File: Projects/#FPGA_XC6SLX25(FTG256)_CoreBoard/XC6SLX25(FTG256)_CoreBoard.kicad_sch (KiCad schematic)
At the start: 148 parts, among them J1 MTA18ASF2G72HZ-2G3A1, U1 XC6SLX25-FTG256, U2 W25Q128JVS, U3 TPS51200DRC, U4 MP214x, U5 MP214x, U6 MP214x, U7 MP214x, X1 ECS-2520MV-xxx-xx

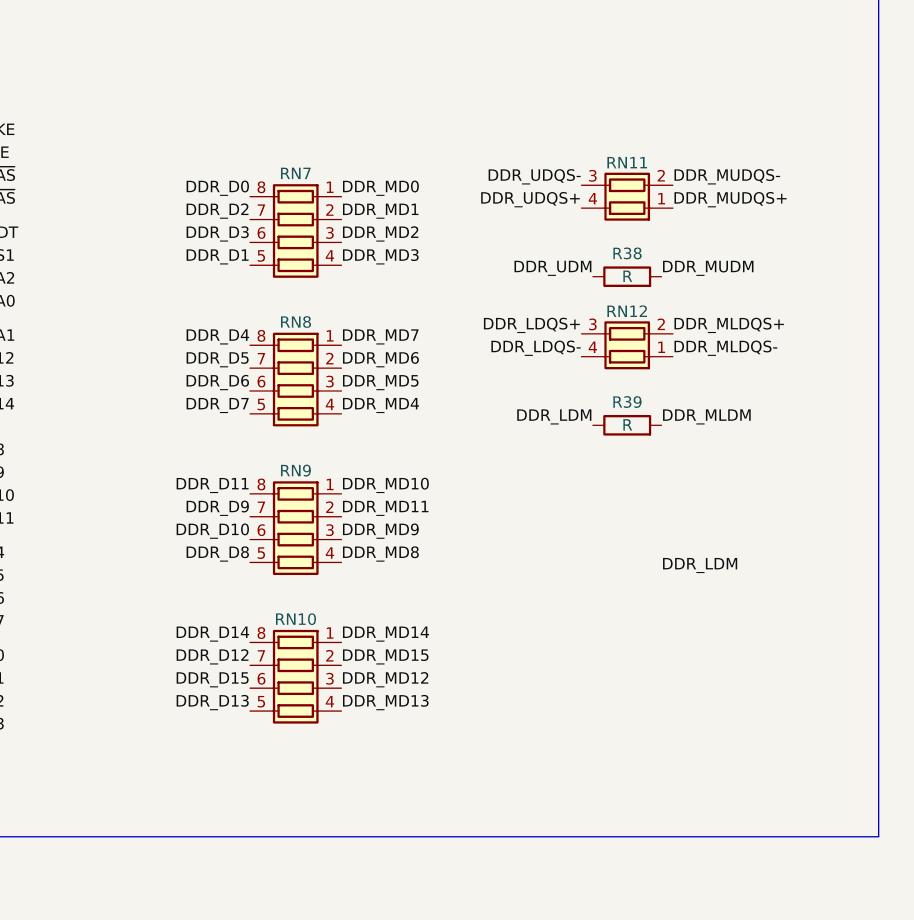
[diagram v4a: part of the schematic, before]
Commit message: Update XC6SLX25(FTG256)_CoreBoard
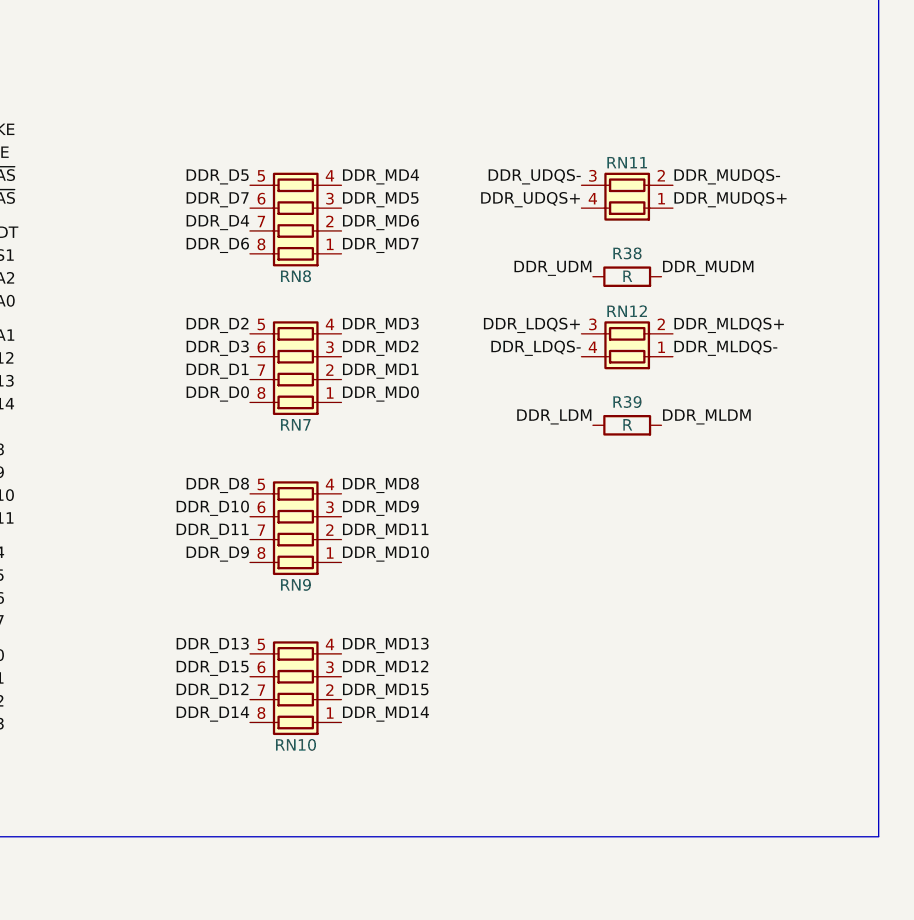
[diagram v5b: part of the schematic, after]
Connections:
- net DDR_D1: now also RN7.7 (R2.2); no longer RN7.5 (R4.2)
- net DDR_D11: now also RN9.7 (R2.2); no longer RN9.8 (R1.2)
- net DDR_D2: now also RN7.5 (R4.2); no longer RN7.7 (R2.2)
- net DDR_D4: now also RN8.7 (R2.2); no longer RN8.8 (R1.2)
- net DDR_D5: now also RN8.5 (R4.2); no longer RN8.7 (R2.2)
- net DDR_D6: now also RN8.8 (R1.2); no longer RN8.6 (R3.2)
- net DDR_D7: now also RN8.6 (R3.2); no longer RN8.5 (R4.2)
- net DDR_D9: now also RN9.8 (R1.2); no longer RN9.7 (R2.2)
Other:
- moved on the sheet: RN10, RN7, RN8

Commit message: Update XC6SLX25(FTG256)_CoreBoard (DDR3 Routing)
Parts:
- removed R38, R39: R, Resistor_SMD:R_0402_1005Metric, symbol Device:R
- added RN13: R_Pack02, Resistor_SMD:R_Array_Convex_2x0402, symbol Device:R_Pack02
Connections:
- net DDR_A1: now also RN2.5 (R4.2); no longer RN1.7 (R2.2)
- net DDR_A10: now also RN5.5 (R4.2); no longer RN3.6 (R3.2)
- net DDR_A11: now also RN2.7 (R2.2); no longer RN3.5 (R4.2)
- net DDR_A12: now also RN2.8 (R1.2); no longer RN4.7 (R2.2)
- net DDR_A13: now also RN1.7 (R2.2); no longer RN4.6 (R3.2)
- net DDR_A14: now also RN2.6 (R3.2); no longer RN4.5 (R4.2)
- net DDR_A2: now also RN1.5 (R4.2); no longer RN1.6 (R3.2)
- net DDR_A3: now also RN6.6 (R3.2); no longer RN1.5 (R4.2)
- net DDR_A4: now also RN4.6 (R3.2); no longer RN2.8 (R1.2)
- net DDR_A5: now also RN6.7 (R2.2); no longer RN2.7 (R2.2)
- net DDR_A6: now also RN4.7 (R2.2); no longer RN2.6 (R3.2)
- net DDR_A7: now also RN6.8 (R1.2); no longer RN2.5 (R4.2)
- net DDR_A8: now also RN4.8 (R1.2); no longer RN3.8 (R1.2)
- net DDR_A9: now also RN1.6 (R3.2); no longer RN3.7 (R2.2)
- net DDR_BA0: now also RN6.5 (R4.2); no longer RN5.5 (R4.2)
- net DDR_BA1: now also RN4.5 (R4.2); no longer RN4.8 (R1.2)
- net DDR_CKE: now also RN3.8 (R1.2); no longer RN6.8 (R1.2)
- net DDR_LDM: now also RN13.4 (R1.2)
- net DDR_MLDM: now also RN13.1 (R1.1)
- net DDR_MUDM: now also RN13.2 (R2.1)
- net DDR_UDM: now also RN13.3 (R2.2)
- net DDR_WE: now also RN3.7 (R2.2); no longer RN6.7 (R2.2)
- net DDR_~{CAS}: now also RN3.6 (R3.2); no longer RN6.6 (R3.2)
- net DDR_~{RAS}: now also RN3.5 (R4.2); no longer RN6.5 (R4.2)

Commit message: Update XC6SLX25(FTG256)_CoreBoard (DDR3 Routing)
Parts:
- added Btn1: SW_Push, Button_Switch_SMD:SW_SPST_CK_RS282G05A3, symbol Switch:SW_Push
- added C26: 0.1uF, Capacitor_SMD:C_0402_1005Metric, symbol Device:C
- added LED1, LED2: LED, LED_SMD:LED_0402_1005Metric, symbol Device:LED
- added R38, R39: 1K, Resistor_SMD:R_0402_1005Metric, symbol Device:R
- added R40: 200R, Resistor_SMD:R_0402_1005Metric, symbol Device:R
- added R41: 100R, Resistor_SMD:R_0402_1005Metric, symbol Device:R
- added SW1: SW_DIP_x01, Button_Switch_SMD:SW_DIP_SPSTx01_Slide_Copal_CHS-01A_W5.08mm_P1.27mm_JPin, symbol Switch:SW_DIP_x01
- R5, R6: value 10K -> 1K
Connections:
- net +3V3: now also R5.1, R6.1, R7.1; no longer R5.2, R6.2, R7.2
- net DDR_A11: now also RN2.6 (R3.2); no longer RN2.7 (R2.2)
- net DDR_A14: now also RN2.7 (R2.2); no longer RN2.6 (R3.2)
- net DDR_A4: now also RN4.7 (R2.2); no longer RN4.6 (R3.2)
- net DDR_A6: now also RN4.6 (R3.2); no longer RN4.7 (R2.2)
- net DDR_A8: now also RN4.5 (R4.2); no longer RN4.8 (R1.2)
- net DDR_BA1: now also RN4.8 (R1.2); no longer RN4.5 (R4.2)
- net DDR_BA2: now also RN3.7 (R2.2); no longer RN5.6 (R3.2)
- net DDR_CKE: now also RN5.6 (R3.2); no longer RN3.8 (R1.2)
- net DDR_CS1: now also RN3.6 (R3.2); no longer RN5.7 (R2.2)
- net DDR_WE: now also RN3.8 (R1.2); no longer RN3.7 (R2.2)
- net DDR_~{CAS}: now also RN5.7 (R2.2); no longer RN3.6 (R3.2)
- net GND: now also C26.1, LED1.1 (K), LED2.1 (K), R40.2, R41.1
- net FPGA_BL_INIT: now reaches U1.R3 (IO_L65P_INIT_B_2)
- net FPGA_BL_INIT: now also R5.2, R38.1; no longer R5.1
- net RESET_FPGA: now reaches U1.T2 (PROGRAM_B_2)
- net RESET_FPGA: now also R7.2, Btn1.1, C26.2; no longer R7.1
- net FPGA_BL_DONE: now reaches U1.P13 (DONE_2)
- net FPGA_BL_DONE: now also R6.2, R39.1, SW1.1; no longer R6.1
- new net: LED2.2 (A), R38.2
- new net: LED1.2 (A), R39.2
- new net: Btn1.2, R41.2
- new net: R40.1, SW1.2
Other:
- note added: "Boot Delay"
- note added: "Loaded Sign"
- note added: "Slaver_mode Deploy Sign"
- note added: "waiting for spi flash loading"
- moved on the sheet: R2, R7, R8, R9, RN11, RN13, U1C, U2, X1

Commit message: Update XC6SLX25(FTG256)_CoreBoard (DDR3 Routing)
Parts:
- removed R40: 200R, Resistor_SMD:R_0402_1005Metric, symbol Device:R
- removed SW1: SW_DIP_x01, Button_Switch_SMD:SW_DIP_SPSTx01_Slide_Copal_CHS-01A_W5.08mm_P1.27mm_JPin, symbol Switch:SW_DIP_x01
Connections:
- net DDR_A0: now also RN2.5 (R4.2); no longer RN1.8 (R1.2)
- net DDR_A1: now also RN5.6 (R3.2); no longer RN2.5 (R4.2)
- net DDR_A10: now also RN4.8 (R1.2); no longer RN5.5 (R4.2)
- net DDR_A11: now also RN6.5 (R4.2); no longer RN2.6 (R3.2)
- net DDR_A12: now also RN5.7 (R2.2); no longer RN2.8 (R1.2)
- net DDR_A13: now also RN3.8 (R1.2); no longer RN1.7 (R2.2)
- net DDR_A14: now also RN6.8 (R1.2); no longer RN2.7 (R2.2)
- net DDR_A2: now also RN2.8 (R1.2); no longer RN1.5 (R4.2)
- net DDR_A3: now also RN2.7 (R2.2); no longer RN6.6 (R3.2)
- net DDR_A4: now also RN5.8 (R1.2); no longer RN4.7 (R2.2)
- net DDR_A5: now also RN3.6 (R3.2); no longer RN6.7 (R2.2)
- net DDR_A6: now also RN6.6 (R3.2); no longer RN4.6 (R3.2)
- net DDR_A7: now also RN3.5 (R4.2); no longer RN6.8 (R1.2)
- net DDR_A8: now also RN6.7 (R2.2); no longer RN4.5 (R4.2)
- net DDR_A9: now also RN3.7 (R2.2); no longer RN1.6 (R3.2)
- net DDR_BA0: now also RN1.8 (R1.2); no longer RN6.5 (R4.2)
- net DDR_BA1: now also RN5.5 (R4.2); no longer RN4.8 (R1.2)
- net DDR_BA2: now also RN2.6 (R3.2); no longer RN3.7 (R2.2)
- net DDR_CKE: now also RN4.7 (R2.2); no longer RN5.6 (R3.2)
- net DDR_CS1: now also RN1.6 (R3.2); no longer RN3.6 (R3.2)
- net DDR_ODT: now also RN1.5 (R4.2); no longer RN5.8 (R1.2)
- net DDR_WE: now also RN1.7 (R2.2); no longer RN3.8 (R1.2)
- net DDR_~{CAS}: now also RN4.6 (R3.2); no longer RN5.7 (R2.2)
- net DDR_~{RAS}: now also RN4.5 (R4.2); no longer RN3.5 (R4.2)
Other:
- moved on the sheet: RN1, RN2, RN3, RN4, RN5, RN6
